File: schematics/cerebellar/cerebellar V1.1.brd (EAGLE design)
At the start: 94.6 x 90.5 mm, 68 parts, among them CON1 ODRV2, CON2 ODRV1, CON3 ODRV3, CON4 ODRV4, CON5 ODRV5, CON6 ODRV6, IC3 LTC7001, P1 Foot1, P11 Foot2, P12 Foot3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

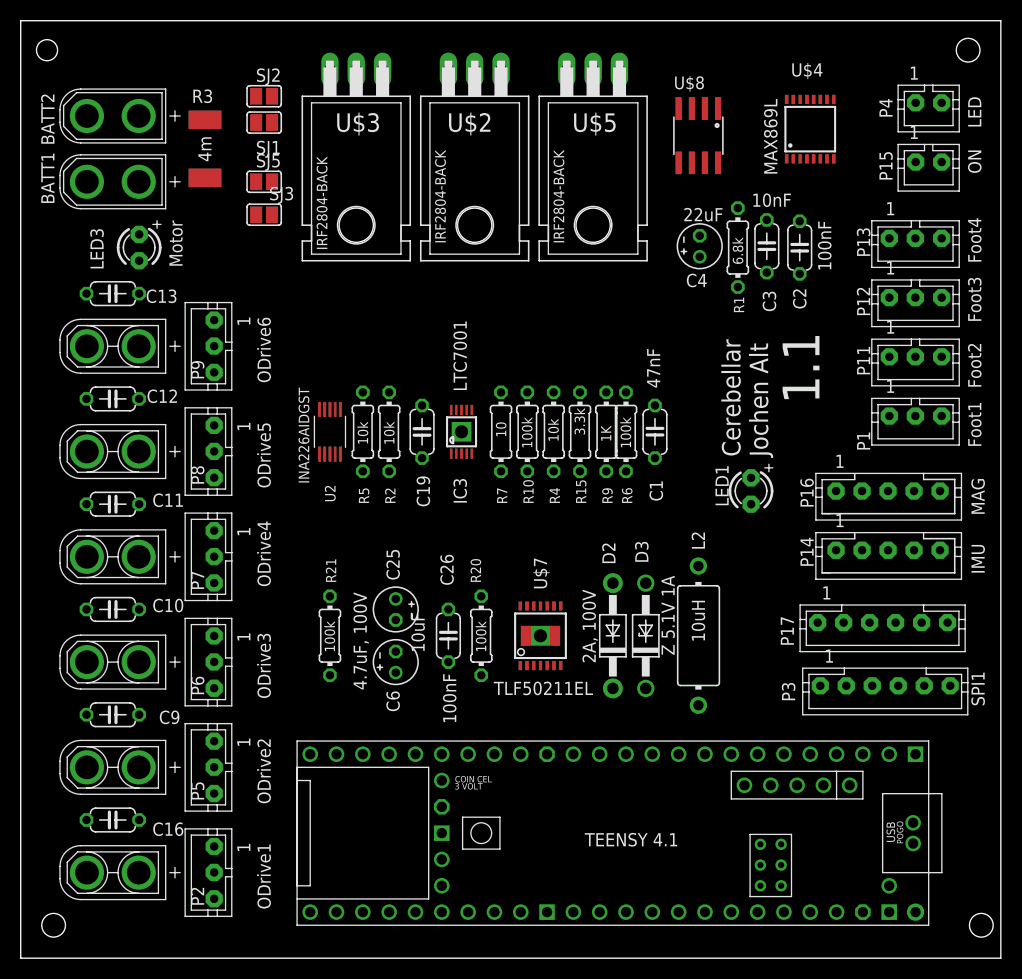
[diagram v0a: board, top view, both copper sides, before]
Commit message: Main Board V3 with 5V 3A power supply for Raspberry
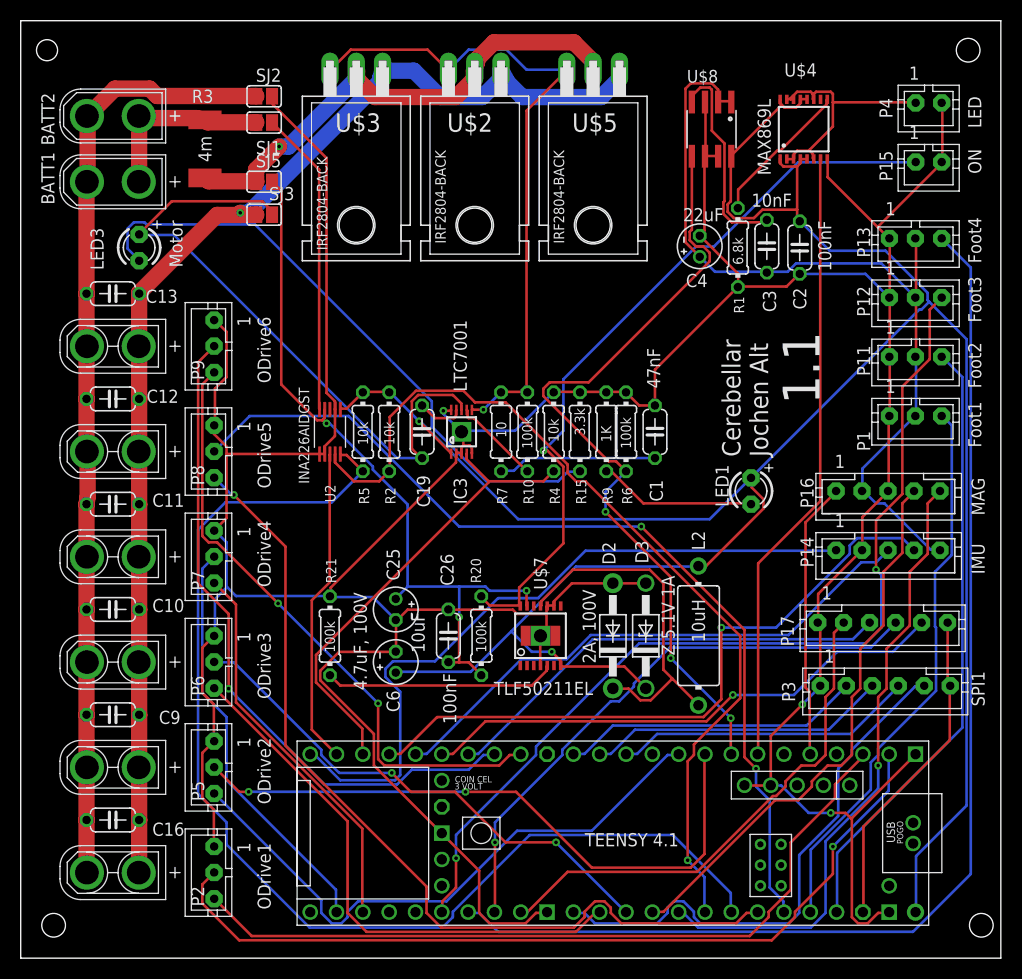
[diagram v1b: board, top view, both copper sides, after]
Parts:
- moved U$8 1.42 mm to (60.3, 80.0)
- moved U$4 0.63 mm to (69.2, 80.0)
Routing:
- net GND: track 0.00 -> 417.0 mm, vias 0 -> 3
- net +5V: track 0.00 -> 248.1 mm, vias 0 -> 2
- net POWER+: track 0.00 -> 118.9 mm, vias 0 -> 1
- net SENS4: track 0.00 -> 114.1 mm
- net N$17: track 0.00 -> 112.8 mm
- net SENS3: track 0.00 -> 92.5 mm, vias 0 -> 2
- net BATT-: track 0.00 -> 90.9 mm
- net O5_RX: track 0.00 -> 90.0 mm, vias 0 -> 2
- net N$22: track 0.00 -> 87.1 mm, vias 0 -> 1
- net O5_TX: track 0.00 -> 86.2 mm, vias 0 -> 1
- net +3.3V: track 0.00 -> 82.8 mm
- net O1_RX: track 0.00 -> 82.5 mm, vias 0 -> 1
- net SHDN: track 0.00 -> 77.4 mm, vias 0 -> 3
- net O1_TX: track 0.00 -> 75.2 mm
- net SWTCH: track 0.00 -> 72.4 mm, vias 0 -> 1
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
